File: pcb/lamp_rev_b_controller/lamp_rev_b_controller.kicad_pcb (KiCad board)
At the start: 4 copper layers, 118 x 94 mm, 155 parts, among them J1 TYPE-C 3.1 MT 16P, J10 2-pin NTC header, J11 2-pin NTC header, J12 DB128H-5.08-2P-BK-S, J13 DB128H-5.08-2P-BK-S, J15 DB128H-5.08-2P-BK-S, J16 LED NTC/ID header, J17 External camera sync header, J18 SPI/FIFO camera module header, J19 Lid/cartridge/cutoff interloc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, J2 DB128H-5.08-2P-BK-S, J20 Fan PWM/tach header, J21 2x3 UART/programming header, J22 I2C expansion header, J23 Analog optical diagnostic hea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, J24 DB128H-5.08-2P high-current h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, J4 2-pin NTC header, J5 2-pin NTC header, J6 2-pin NTC header, J7 2-pin NTC header, J8 2-pin NTC header, J9 2-pin NTC header, Q1 IRLB3813PBF TO-220 12V protot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, Q2 IRLB3813PBF TO-220 12V protot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, U1 ESP32-S3-WROOM-1-N16, U10 INA180A1IDBVR gain 20 LED cur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, U2 USBLC6-2SC6, U3 Diodes AP63203WU-7 fixed 3.3V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, U4 ADS1115IDGSR, U5 CD74HC4051M, U6 TC4427ACOA/TC4427EPA, U7 CUI/Bel P7805-2000-S 5V 2A 8-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, U8 Mean Well LDD-700H 700mA CC b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, U9 SN74LVC1G08DBVR LED_EXC_PWM A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

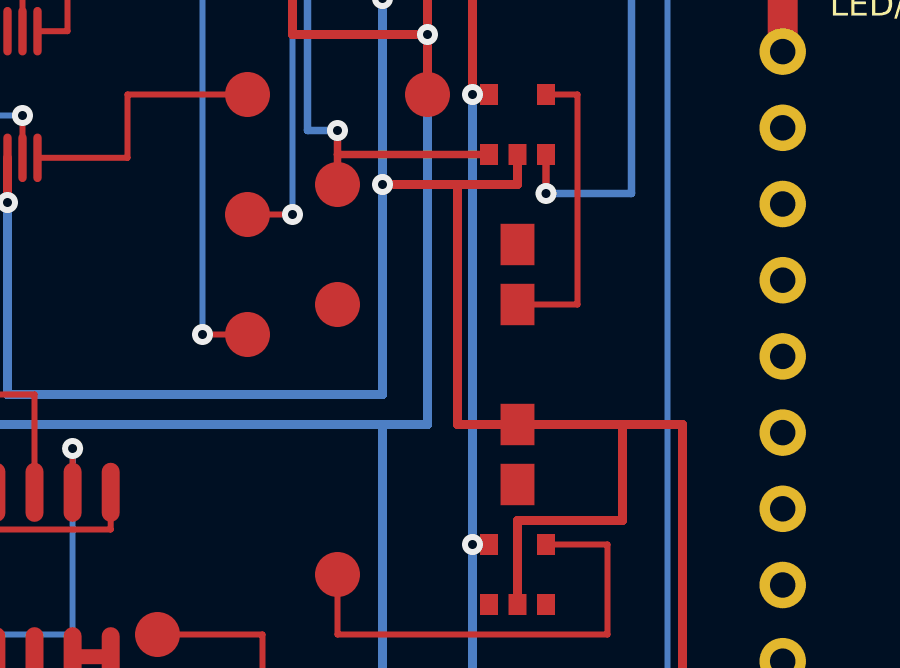
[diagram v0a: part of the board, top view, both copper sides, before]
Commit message: Close LED_DIM_DRIVE route on Rev B controller
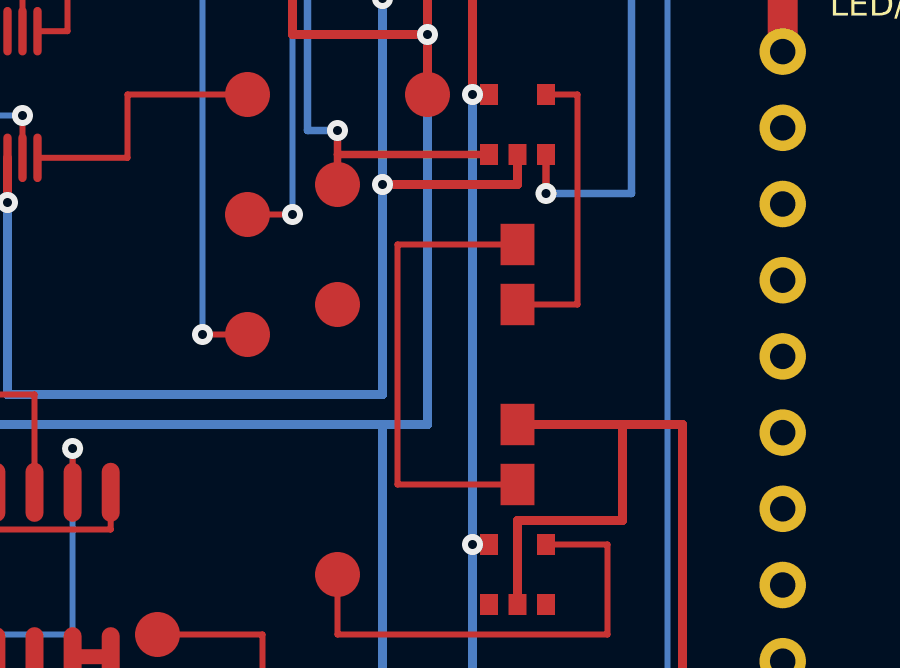
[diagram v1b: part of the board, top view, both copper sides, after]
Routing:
- net LED_DIM_DRIVE: track 0.00 -> 16.0 mm
- net GND: track 348.8 -> 341.3 mm
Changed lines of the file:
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@@
+  )
+  (segment
+    (start 47 47)
+    (end 43 47)
+    (width 0.200)
+    (layer "F.Cu")
+    (net 52)
+  )
+  (segment
+    (start 43 47)
+    (end 43 55)
+    (width 0.200)
+    (layer "F.Cu")
+    (net 52)
+  )
+  (segment
+    (start 43 55)
+    (end 47 55)
+    (width 0.200)
+    (layer "F.Cu")
+    (net 52)
   )
   (segment
@@
   (segment
     (start 45 45)
-    (end 45 53)
-    (width 0.300)
-    (layer "F.Cu")
-    (net 1)
-  )
-  (segment
-    (start 45 53)
-    (end 47 53)
-    (width 0.300)
-    (layer "F.Cu")
+    (end 42.500 45)
+    (width 0.300)
+    (layer "F.Cu")

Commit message: Close HEATER0_PWM U6 route on Rev B controller
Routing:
- net HEATER0_PWM: track 13.0 -> 17.8 mm
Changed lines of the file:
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@@
+  )
+  (segment
+    (start 92.200 54.500)
+    (end 92.200 52)
+    (width 0.250)
+    (layer "F.Cu")
+    (net 33)
+  )
+  (segment
+    (start 92.200 52)
+    (end 91.370 52)
+    (width 0.250)
+    (layer "F.Cu")
+    (net 33)
+  )
+  (segment
+    (start 91.370 52)
+    (end 91.370 50.570)
+    (width 0.250)
+    (layer "F.Cu")
+    (net 33)
   )
   (segment

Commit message: Route HEATER1_LOW Q2 trunk drop
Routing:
- net HEATER1_LOW: track 42.1 -> 55.6 mm
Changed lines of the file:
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@@
+  )
+  (segment
+    (start 113.540 49)
+    (end 113.540 62)
+    (width 1.200)
+    (layer "F.Cu")
+    (net 38)
+  )
+  (segment
+    (start 113.540 62)
+    (end 113 62)
+    (width 1.200)
+    (layer "F.Cu")
+    (net 38)
   )
   (segment

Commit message: Route HEATER1_GATE TP jog closure
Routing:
- net HEATER1_GATE: track 23.6 -> 44.1 mm
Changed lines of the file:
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@@
+  )
+  (segment
+    (start 97.500 61)
+    (end 97.500 56.800)
+    (width 0.300)
+    (layer "F.Cu")
+    (net 36)
+  )
+  (segment
+    (start 97.500 56.800)
+    (end 104.500 56.800)
+    (width 0.300)
+    (layer "F.Cu")
+    (net 36)
+  )
+  (segment
+    (start 104.500 56.800)
+    (end 104.500 52)
+    (width 0.300)
+    (layer "F.Cu")
+    (net 36)
+  )
+  (segment
+    (start 104.500 52)
+    (end 109 52)
+    (width 0.300)
+    (layer "F.Cu")
+    (net 36)
   )
   (segment

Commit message: Add LATCH_LOCKED_N Rev B seed route
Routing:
- net LATCH_LOCKED_N: track 0.00 -> 10.0 mm
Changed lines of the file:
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@@
+  )
+  (segment
+    (start 54.080 84)
+    (end 54.080 83.415)
+    (width 0.200)
+    (layer "F.Cu")
+    (net 64)
+  )
+  (segment
+    (start 54.080 83.415)
+    (end 59 78.495)
+    (width 0.200)
+    (layer "F.Cu")
+    (net 64)
+  )
+  (segment
+    (start 59 78.495)
+    (end 59 76)
+    (width 0.200)
+    (layer "F.Cu")
+    (net 64)
   )
   (segment

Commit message: Route Rev B THERM_CH_2 branch
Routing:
- net THERM_CH_2: track 0.00 -> 32.4 mm
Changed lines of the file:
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@@
     (net 22)
+  )
+  (segment
+    (start 25.820 55.260)
+    (end 25.820 54.023)
+    (width 0.200)
+    (layer "F.Cu")
+    (net 74)
+  )
+  (segment
+    (start 25.820 54.023)
+    (end 17.451 54.023)
+    (width 0.200)
+    (layer "F.Cu")
+    (net 74)
+  )
+  (segment
+    (start 17.451 54.023)
+    (end 15.330 56.145)
+    (width 0.200)
+    (layer "F.Cu")
+    (net 74)
+  )
+  (segment
+    (start 15.330 56.145)
+    (end 11.825 56.145)
+    (width 0.200)
+    (layer "F.Cu")
+    (net 74)
+  )
+  (segment
+    (start 11.825 56.145)
+    (end 10.957 57.013)
+    (width 0.200)
+    (layer "F.Cu")
+    (net 74)
+  )
+  (segment
+    (start 10.957 57.013)
+    (end 10.957 64.957)
+    (width 0.200)
+    (layer "F.Cu")
+    (net 74)
+  )
+  (segment
+    (start 10.957 64.957)
+    (end 16 70)
+    (width 0.200)
+    (layer "F.Cu")
+    (net 74)
   )
   (zone

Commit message: Promote Rev B CAM_PWDN_N route
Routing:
- net CAM_PWDN_N: track 0.00 -> 28.9 mm
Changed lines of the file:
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@@
+  )
+  (segment
+    (start 94 72)
+    (end 85.730 80.270)
+    (width 0.200)
+    (layer "F.Cu")
+    (net 30)
+  )
+  (segment
+    (start 85.730 80.270)
+    (end 70.350 80.270)
+    (width 0.200)
+    (layer "F.Cu")
+    (net 30)
+  )
+  (segment
+    (start 70.350 80.270)
+    (end 69.080 81.540)
+    (width 0.200)
+    (layer "F.Cu")
+    (net 30)
   )
   (segment

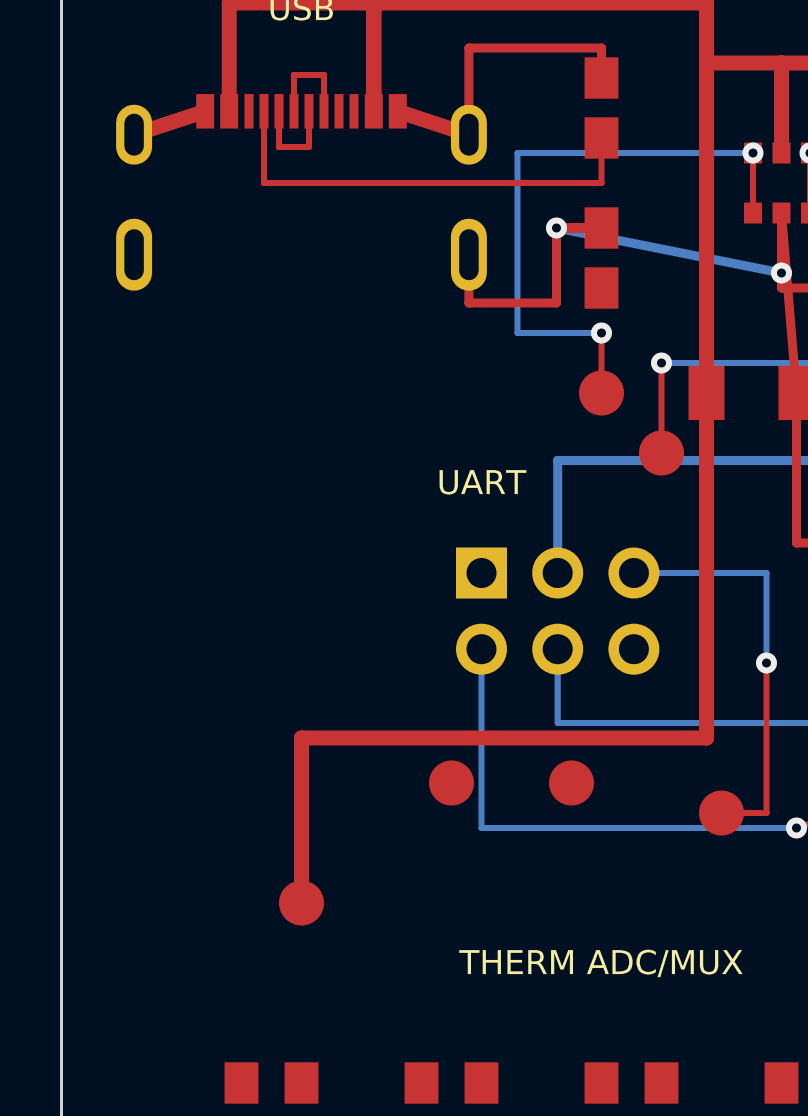
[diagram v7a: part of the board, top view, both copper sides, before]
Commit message: Close USB_CC1 Rev B controller route
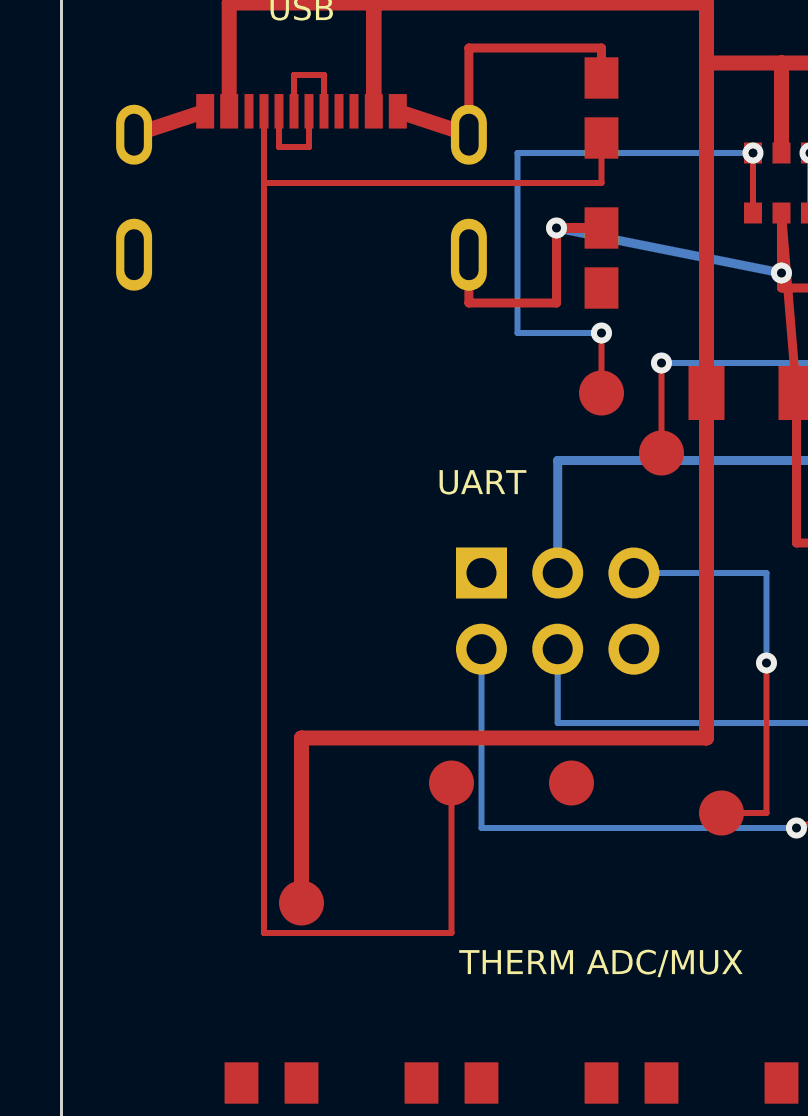
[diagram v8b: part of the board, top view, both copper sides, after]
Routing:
- net USB_CC1: track 15.1 -> 51.4 mm
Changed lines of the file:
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@@
+  )
+  (segment
+    (start 13 28)
+    (end 13 33)
+    (width 0.200)
+    (layer "F.Cu")
+    (net 15)
+  )
+  (segment
+    (start 13 33)
+    (end 6.750 33)
+    (width 0.200)
+    (layer "F.Cu")
+    (net 15)
+  )
+  (segment
+    (start 6.750 33)
+    (end 6.750 8)
+    (width 0.200)
+    (layer "F.Cu")
+    (net 15)
   )
   (segment
